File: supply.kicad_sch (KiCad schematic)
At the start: 0 parts

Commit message: [#52579] Add PAC1934 and connect it to SoC
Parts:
- added U?: PAC1934_QFN, antmicro-footprints:QFN-16-1EP_4x4mm_P0.65mm, symbol antmicroMicrocontrollers:PAC1934_QFN
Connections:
- new net PAC1934_SCL: U?.4 (SM_CLK)
- new net PAC1934_SDA: U?.5 (SM_DATA)
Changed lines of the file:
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@@
 (kicad_sch (version 20211123) (generator eeschema)
   (paper "A4")
+  (wire (pts (xy 46.99 60.96) (xy 52.07 60.96))
+    (stroke (width 0) (type default) (color 0 0 0 0))
+  )
+  (wire (pts (xy 46.99 58.42) (xy 52.07 58.42))
+    (stroke (width 0) (type default) (color 0 0 0 0))
+  )
+  (global_label "PAC1934_SDA" (shape input) (at 46.99 60.96 180) (fields_autoplaced)
+    (effects (font (size 1.27 1.27)) (justify right))
+    (property "Intersheet References" "${INTERSHEET_REFS}" (id 0) (at 31.5745 60.8806 0)
+      (effects (font (size 1.27 1.27)) (justify right) hide)
+    )
+  )
+  (global_label "PAC1934_SCL" (shape input) (at 46.99 58.42 180) (fields_autoplaced)
+    (effects (font (size 1.27 1.27)) (justify right))
+    (property "Intersheet References" "${INTERSHEET_REFS}" (id 0) (at 31.635 58.3406 0)
+      (effects (font (size 1.27 1.27)) (justify right) hide)
+    )
+  )
+  (symbol (lib_id "antmicroMicrocontrollers:PAC1934_QFN") (at 52.07 53.34 0) (unit 1)
+    (in_bom yes) (on_board yes) (fields_autoplaced)
+    (property "Reference" "U?" (id 0) (at 66.04 45.72 0)
+      (effects (font (size 1.27 1.27) (thickness 0.15)))
+    )
+    (property "Value" "PAC1934_QFN" (id 1) (at 95.25 60.96 0)
+      (effects (font (size 1.27 1.27) (thickness 0.15)) (justify left bottom) hide)
+    )
+    (property "Footprint" "antmicro-footprints:QFN-16-1EP_4x4mm_P0.65mm" (id 2) (at 95.25 63.5 0)
+      (effects (font (size 1.27 1.27) (thickness 0.15)) (justify left bottom) hide)
+    )
+    (property "Datasheet" "https://www.mouser.com/datasheet/2/268/PAC1931_Family_Data_Sheet_DS20005850E-1519053.pdf" (id 3) (at 95.25 66.04 0)
+      (effects (font (size 1.27 1.27) (thickness 0.15)) (justify left bottom) hide)
+    )
+    (property "MPN" "PAC1934T-I/JQ" (id 4) (at 66.04 48.26 0)
+      (effects (font (size 1.27 1.27) (thickness 0.15)))
+    )
+    (property "Manufacturer" "Microchip Technology" (id 5) (at 95.25 68.58 0)
+      (effects (font (size 1.27 1.27) (thickness 0.15)) (justify left bottom) hide)
+    )
+    (property "Author" "Antmicro" (id 6) (at 95.25 73.66 0)
+      (effects (font (size 1.27 1.27) (thickness 0.15)) (justify left bottom) hide)
+    )
+    (property "License" "Apache-2.0" (id 7) (at 95.25 76.2 0)
+      (effects (font (size 1.27 1.27) (thickness 0.15)) (justify left bottom) hide)
+    )
+    (pin "1")
+    (pin "10")
+    (pin "11")
+    (pin "12")
+    (pin "13")
+    (pin "14")
+    (pin "15")
+    (pin "16")
+    (pin "17")
+    (pin "2")
+    (pin "3")
+    (pin "4")
+    (pin "5")
+    (pin "6")
+    (pin "7")
+    (pin "8")
+    (pin "9")
+  )
 )

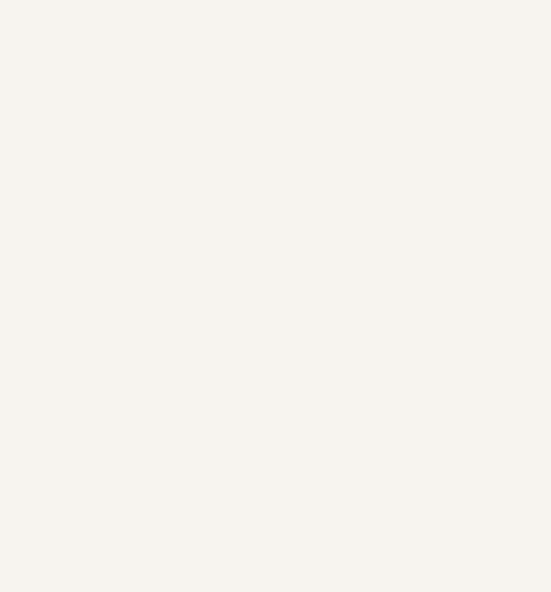
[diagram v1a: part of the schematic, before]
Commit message: [#52579] Add and connect SPI FLASH
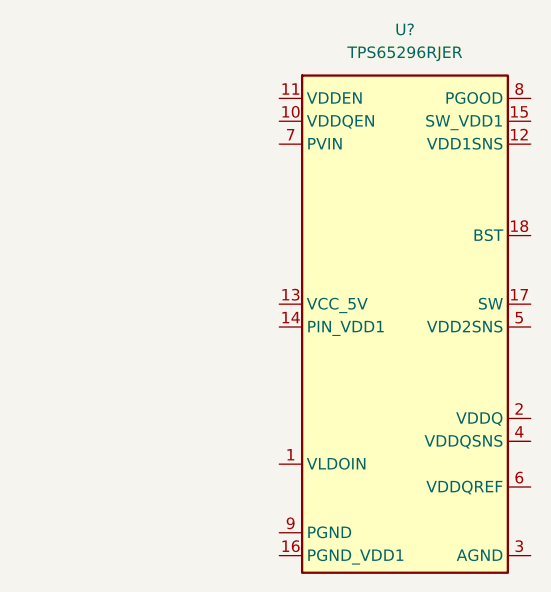
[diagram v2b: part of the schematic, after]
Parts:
- added U?: TPS65296, antmicro-footprints:VQFN-HR-18_3.5x3.5x1mm, symbol antmicroPMICVoltageRegulatorsDCDCSwitchingControllers:TPS65296
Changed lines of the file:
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@@
     )
+  )
+  (symbol (lib_id "antmicroPMICVoltageRegulatorsDCDCSwitchingControllers:TPS65296") (at 184.15 53.34 0) (unit 1)
+    (in_bom yes) (on_board yes) (fields_autoplaced)
+    (property "Reference" "U?" (id 0) (at 198.12 45.72 0)
+      (effects (font (size 1.27 1.27) (thickness 0.15)))
+    )
+    (property "Value" "TPS65296" (id 1) (at 224.79 60.96 0)
+      (effects (font (size 1.27 1.27) (thickness 0.15)) (justify left bottom) hide)
+    )
+    (property "Footprint" "antmicro-footprints:VQFN-HR-18_3.5x3.5x1mm" (id 2) (at 224.79 63.5 0)
+      (effects (font (size 1.27 1.27) (thickness 0.15)) (justify left bottom) hide)
+    )
+    (property "Datasheet" "https://www.ti.com/lit/ds/symlink/tps65296.pdf" (id 3) (at 224.79 66.04 0)
+      (effects (font (size 1.27 1.27) (thickness 0.15)) (justify left bottom) hide)
+    )
+    (property "Manufacturer" "Texas Instruments" (id 4) (at 224.79 68.58 0)
+      (effects (font (size 1.27 1.27) (thickness 0.15)) (justify left bottom) hide)
+    )
+    (property "MPN" "TPS65296RJER" (id 5) (at 198.12 48.26 0)
+      (effects (font (size 1.27 1.27) (thickness 0.15)))
+    )
+    (property "Author" "Antmicro" (id 6) (at 224.79 71.12 0)
+      (effects (font (size 1.27 1.27) (thickness 0.15)) (justify left bottom) hide)
+    )
+    (property "License" "Apache-2.0" (id 7) (at 224.79 73.66 0)
+      (effects (font (size 1.27 1.27) (thickness 0.15)) (justify left bottom) hide)
+    )
+    (pin "1")
+    (pin "10")
+    (pin "11")
+    (pin "12")
+    (pin "13")
+    (pin "14")
+    (pin "15")
+    (pin "16")
+    (pin "17")
+    (pin "18")
+    (pin "2")
+    (pin "3")
+    (pin "4")
+    (pin "5")
+    (pin "6")
+    (pin "7")
+    (pin "8")
+    (pin "9")
   )
   (symbol (lib_id "antmicroMicrocontrollers:PAC1934_QFN") (at 52.07 53.34 0) (unit 1)

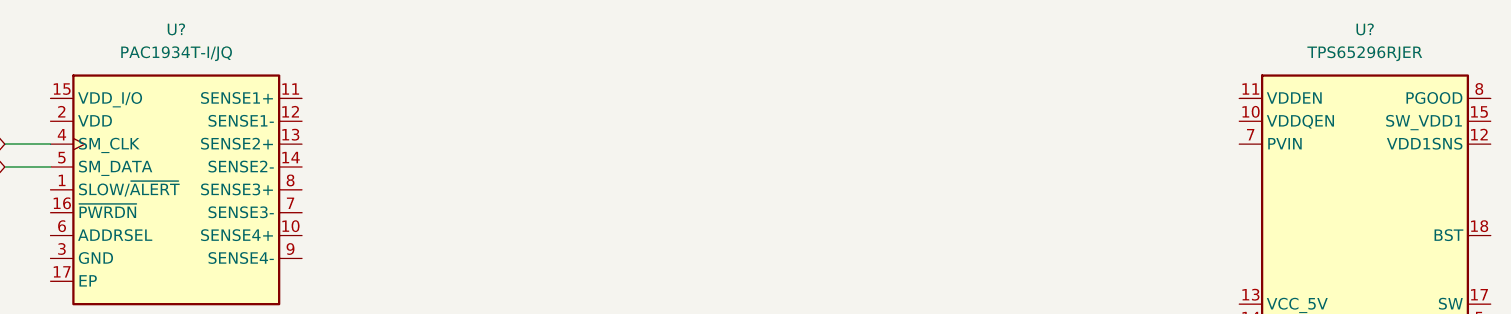
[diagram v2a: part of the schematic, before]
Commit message: [#52579] Connect CSI and DSI to CrossLink
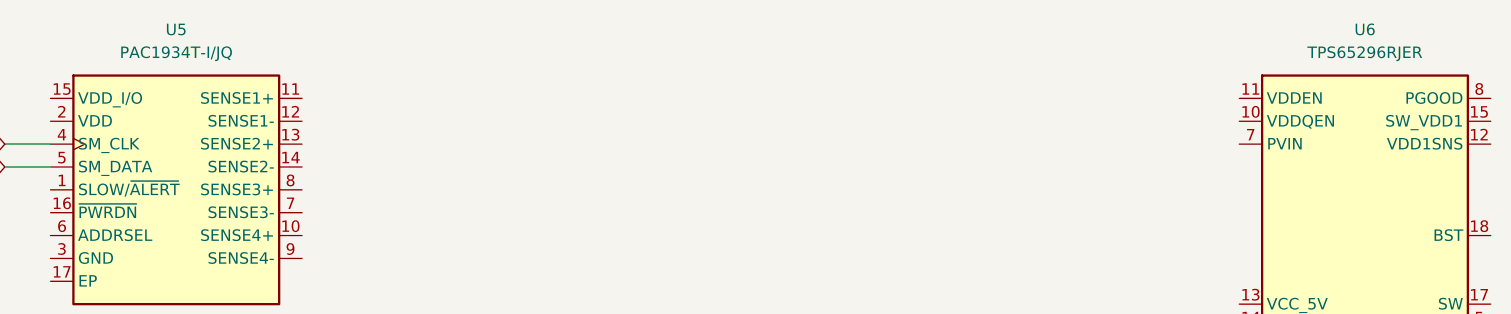
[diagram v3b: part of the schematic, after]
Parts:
- gave numbers to parts that had none: 2
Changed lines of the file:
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@@
   (symbol (lib_id "antmicroPMICVoltageRegulatorsDCDCSwitchingControllers:TPS65296") (at 184.15 53.34 0) (unit 1)
     (in_bom yes) (on_board yes) (fields_autoplaced)
-    (property "Reference" "U?" (id 0) (at 198.12 45.72 0)
+    (property "Reference" "U6" (id 0) (at 198.12 45.72 0)
       (effects (font (size 1.27 1.27) (thickness 0.15)))
     )
@@
   (symbol (lib_id "antmicroMicrocontrollers:PAC1934_QFN") (at 52.07 53.34 0) (unit 1)
     (in_bom yes) (on_board yes) (fields_autoplaced)
-    (property "Reference" "U?" (id 0) (at 66.04 45.72 0)
+    (property "Reference" "U5" (id 0) (at 66.04 45.72 0)
       (effects (font (size 1.27 1.27) (thickness 0.15)))
     )

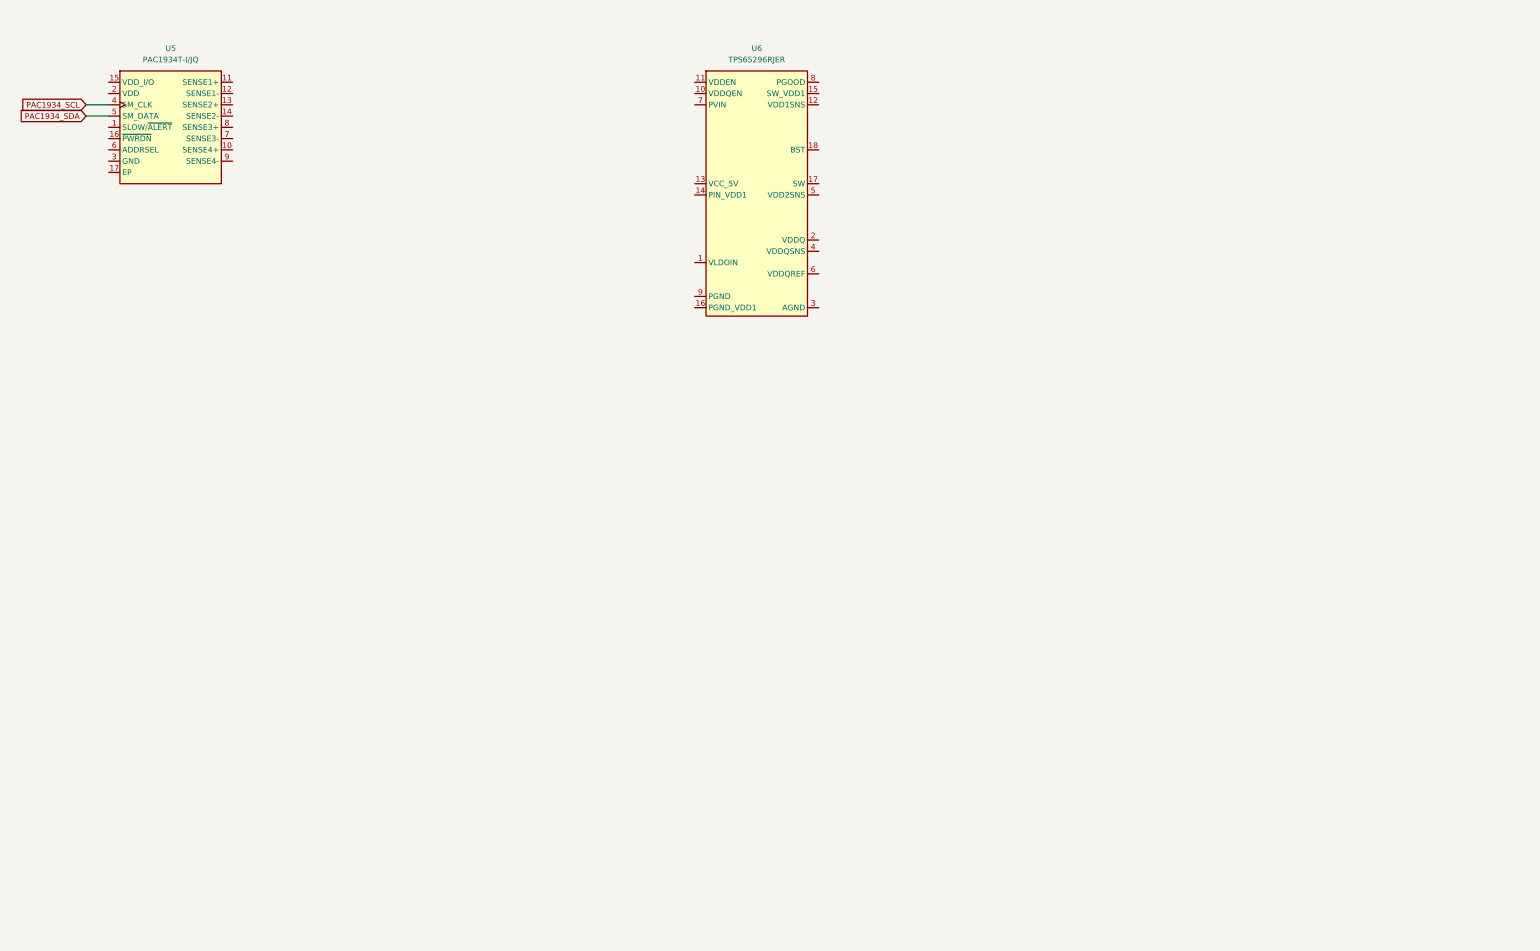
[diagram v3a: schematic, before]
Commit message: [#52577] Add PMIC with adjacent components
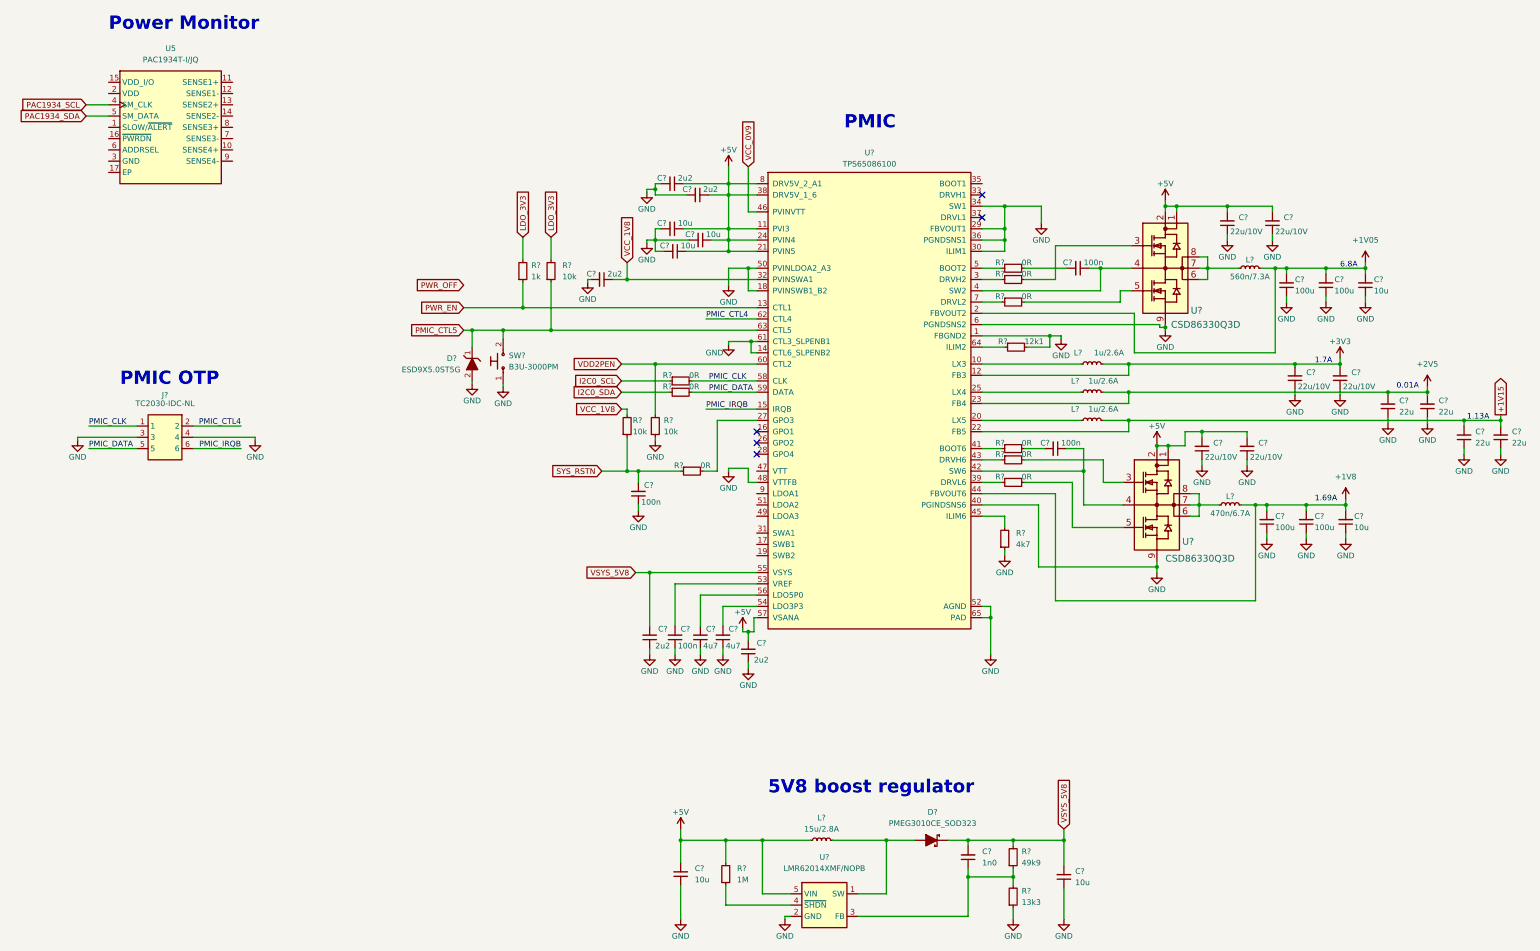
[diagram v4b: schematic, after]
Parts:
- removed U6: TPS65296, antmicro-footprints:VQFN-HR-18_3.5x3.5x1mm, symbol antmicroPMICVoltageRegulatorsDCDCSwitchingControllers:TPS65296
- added C?: C_1n0_0402, antmicro-footprints:C_0402_1005Metric, symbol antmicroCapacitors0402:C_1n0_0402
- added C? (x2): C_10u_0402, antmicro-footprints:C_0402_1005Metric, symbol antmicroCapacitors0402:C_10u_0402
- added C? (x4): C_22u_0402, antmicro-footprints:C_0402_1005Metric, symbol antmicroCapacitors0402:C_22u_0402
- added C? (x5): C_10u_10V_0402, antmicro-footprints:C_0402_1005Metric, symbol antmicroCapacitors0402:C_10u_10V_0402
- added C? (x5): C_2u2_0402, antmicro-footprints:C_0402_1005Metric, symbol antmicroCapacitors0402:C_2u2_0402
- added C? (x6): C_22u_10V_0603, antmicro-footprints:C_0603_1608Metric, symbol antmicroCapacitors0603:C_22u_10V_0603
- added C? (x4): C_100n_0402, antmicro-footprints:C_0402_1005Metric, symbol antmicroCapacitors0402:C_100n_0402
- added C? (x4): C_100u_0805, antmicro-footprints:C_0805_2012Metric, symbol antmicroCapacitorsmisc:C_100u_0805
- added C? (x2): C_4u7_0402, antmicro-footprints:C_0402_1005Metric, symbol antmicroCapacitors0402:C_4u7_0402
- added D?: PMEG3010CE_SOD323, antmicro-footprints:D_SOD-323F, symbol antmicroDiodesRectifiersSingle:PMEG3010CE_SOD323
- added D?: ESD9X5.0ST5G, antmicro-footprints:SOD-923, symbol antmicroTVSDiodes:ESD9X5.0ST5G
- added J?: Tag-Connect_TC2030-IDC-NL_2x3_P1.27mm, antmicro-footprints:Tag-Connect_TC2030-IDC-NL_2x3_P1.27mm, symbol antmicroTestPoints:Tag-Connect_TC2030-IDC-NL_2x3_P1.27mm
- added L?: L_560n_7.3A_Bourns-SRP4020, antmicro-footprints:L_Bourns-SRP4020, symbol antmicroFixedInductors:L_560n_7.3A_Bourns-SRP4020
- added L?: L_470n_6.7A_Vishay-IHLP-1212AE-11, antmicro-footprints:L_Vishay-IHLP-1212AE, symbol antmicroFixedInductors:L_470n_6.7A_Vishay-IHLP-1212AE-11
- added L? (x3): L_1u_2.6A_0806, antmicro-footprints:L_0806_2016Metric, symbol antmicroFixedInductors:L_1u_2.6A_0806
- added L?: L_15u_2.8A_Coilcraft-XAL4040, antmicro-footprints:L_Coilcraft-XAL4040, symbol antmicroFixedInductors:L_15u_2.8A_Coilcraft-XAL4040
- added R? (x9): R_0R_0402, antmicro-footprints:R_0402_1005Metric, symbol antmicroResistors0402:R_0R_0402
- added R? (x3): R_10k_0402, antmicro-footprints:R_0402_1005Metric, symbol antmicroResistors0402:R_10k_0402
- added R?: R_12k1_0402, antmicro-footprints:R_0402_1005Metric, symbol antmicroResistors0402:R_12k1_0402
- added R?: R_49k9_0402, antmicro-footprints:R_0402_1005Metric, symbol antmicroResistors0402:R_49k9_0402
- added R?: R_13k3_0402, antmicro-footprints:R_0402_1005Metric, symbol antmicroResistors0402:R_13k3_0402
- added R?: R_1k_0402, antmicro-footprints:R_0402_1005Metric, symbol antmicroResistors0402:R_1k_0402
- added R?: R_4k7_0402, antmicro-footprints:R_0402_1005Metric, symbol antmicroResistors0402:R_4k7_0402
- added R?: R_1M_0402, antmicro-footprints:R_0402_1005Metric, symbol antmicroResistors0402:R_1M_0402
- added SW?: SW_B3U-3000PM_SMD, antmicro-footprints:SW_B3U-3000PM_SMD, symbol antmicroPushbuttonSwitches:SW_B3U-3000PM_SMD
- added U?: TPS65086100, antmicro-footprints:QFN50P900X900X80-65N, symbol antmicroPMICBatteryManagement:TPS65086100
- added U? (x2): CSD86330Q3D, antmicro-footprints:CSD86330Q3D, symbol antmicroTransistorsFETsMOSFETsArrays:CSD86330Q3D
- added U?: LMR62014XMF, antmicro-footprints:SOT-23-5, symbol antmicroDCDCConverters:LMR62014XMF
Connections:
- new net: C?.1, R?.1, R?.2, U?.3 (FB)
- new net: L?.1, U?.6 (VSW), U?.7 (VSW), U?.8 (VSW) (x2)
- new net: R?.1, U?.5 (BOOT2)
- new net: C?.2, R?.2 (x2)
- new net: R?.1, U?.43 (DRVH6)
- new net: R?.2, U?.3 (TG) (x2)
- new net: R?.1, U?.3 (DRVH2)
- new net: L?.1, U?.10 (LX3)
- new net: L?.1, U?.20 (LX5)
- new net: L?.1, U?.25 (LX4)
- new net: R?.2, U?.27 (GPO3)
- new net: R?.1, U?.39 (DRVL6)
- new net: C?.1, U?.4 (SW2), U?.4 (TGR)
- new net: R?.1, U?.41 (BOOT6)
- new net: C?.1, U?.4 (TGR), U?.42 (SW6)
- new net: R?.2, U?.45 (ILIM6)
- new net: C?.2, U?.53 (VREF)
- new net: C?.2, U?.54 (LDO3P3)
- new net: C?.2, U?.56 (LDO5P0)
- new net: R?.1, U?.64 (ILIM2)
- new net: R?.1, U?.7 (DRVL2)
- new net: R?.2, U?.5 (BG) (x2)
- new net: D?.A, L?.2, U?.1 (SW)
- new net: R?.1, U?.4 (~{SHDN})
- new net +1V05: C?.2, C?.2, C?.2, L?.2, U?.2 (FBVOUT2)
- new net +1V15: C?.2, C?.2, L?.2, U?.22 (FB5)
- new net +1V8: C?.2, C?.2, C?.2, L?.2, U?.44 (FBVOUT6)
- new net +2V5: C?.2, C?.2, L?.2, U?.23 (FB4)
- new net +3V3: C?.2, C?.2, L?.2, U?.12 (FB3)
- new net +5V: C?.1, C?.1, C?.1, C?.1, C?.1, C?.2, C?.2, C?.2, C?.2, C?.2, C?.2, L?.1, R?.2, U?.1 (VIN), U?.1 (VIN), U?.11 (PVI3), U?.2 (VIN), U?.2 (VIN), U?.21 (PVIN5), U?.24 (PVIN4), U?.38 (DRV5V_1_6), U?.5 (VIN), U?.57 (VSANA), U?.8 (DRV5V_2_A1)
- new net GND: C?.1, C?.1, C?.1, C?.1, C?.1, C?.1, C?.1, C?.1, C?.1, C?.1, C?.1, C?.1, C?.1, C?.1, C?.1, C?.1, C?.1, C?.1, C?.1, C?.1, C?.1, C?.1, C?.1, C?.1, C?.2, C?.2, C?.2, C?.2, C?.2, C?.2, D?.2, J?.3, J?.4, R?.1, R?.1, R?.1, R?.2, SW?.1, U?.1 (FBGND2), U?.14 (CTL6_SLPENB2), U?.18 (PVINSWB1_B2), U?.2 (GND), U?.29 (FBVOUT1), U?.30 (ILIM1), U?.34 (SW1), U?.36 (PGNDSNS1), U?.40 (PGINDSNS6), U?.48 (VTTFB), U?.50 (PVINLDOA2_A3), U?.52 (AGND), U?.6 (PGNDSNS2), U?.61 (CTL3_SLPENB1), U?.65 (PAD), U?.9 (PGND), U?.9 (PGND)
- new net I2C0_SCL: R?.1
- new net I2C0_SDA: R?.1
- new net LDO_3V3: R?.2, R?.2
- new net PMIC_CLK: J?.1, R?.2, U?.58 (CLK)
- new net PMIC_CTL4: J?.2, U?.62 (CTL4)
- new net PMIC_CTL5: D?.1, R?.1, SW?.2, U?.63 (CTL5)
- new net PMIC_DATA: J?.5, R?.2, U?.59 (DATA)
- new net PMIC_IRQB: J?.6, U?.15 (IRQB)
- new net PWR_EN: R?.1, U?.13 (CTL1)
- new net SYS_RSTN: C?.2, R?.1, R?.1
- new net VCC_0V9: U?.46 (PVINVTT)
- new net VCC_1V8: C?.1, R?.2, U?.32 (PVINSWA1)
- new net VDD2PEN: R?.2, U?.60 (CTL2)
- new net VSYS_5V8: C?.2, C?.2, C?.2, D?.K, R?.2, U?.55 (VSYS)
- no-connect marks 0 -> 5
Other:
- note added: "0.01A"
- note added: "1.13A"
- note added: "1.69A"
- note added: "1.7A"
- note added: "5V8 boost regulator"
- note added: "6.8A"
- note added: "PMIC"
- note added: "PMIC OTP"
- note added: "Power Monitor"
- title: (none) -> PolarFire SoM
